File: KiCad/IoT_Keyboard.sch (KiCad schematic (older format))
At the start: 3 parts, among them SW1 SW_Push, U1 Elite-C

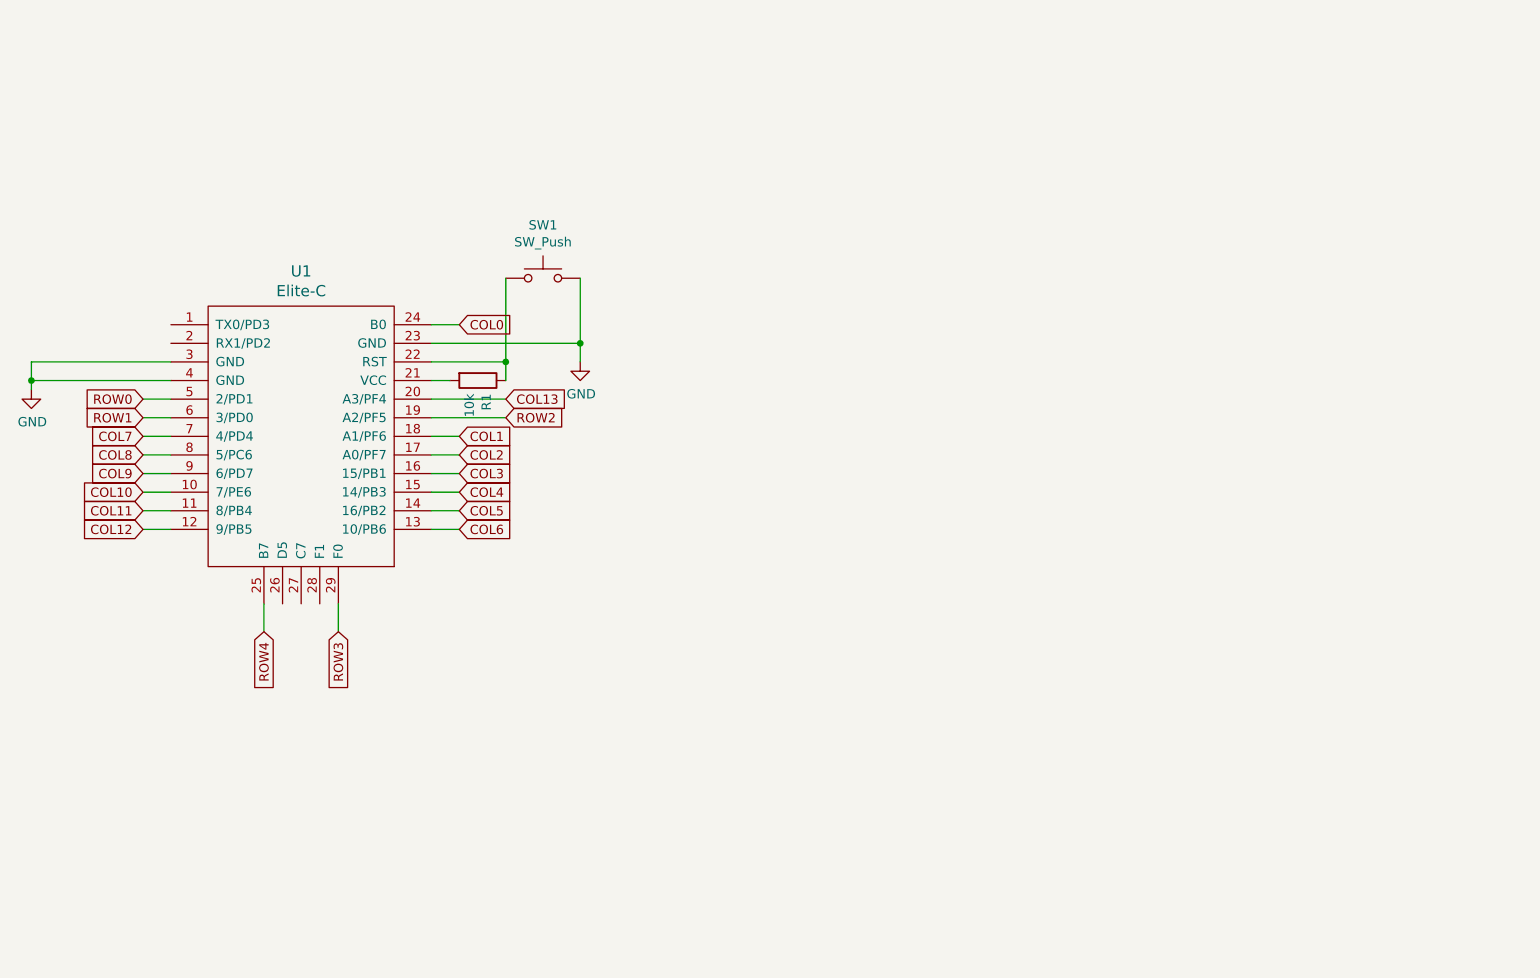
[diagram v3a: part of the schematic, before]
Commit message: Added HC-05 to PCB and routed. Added mounting holes. Generated gerbers
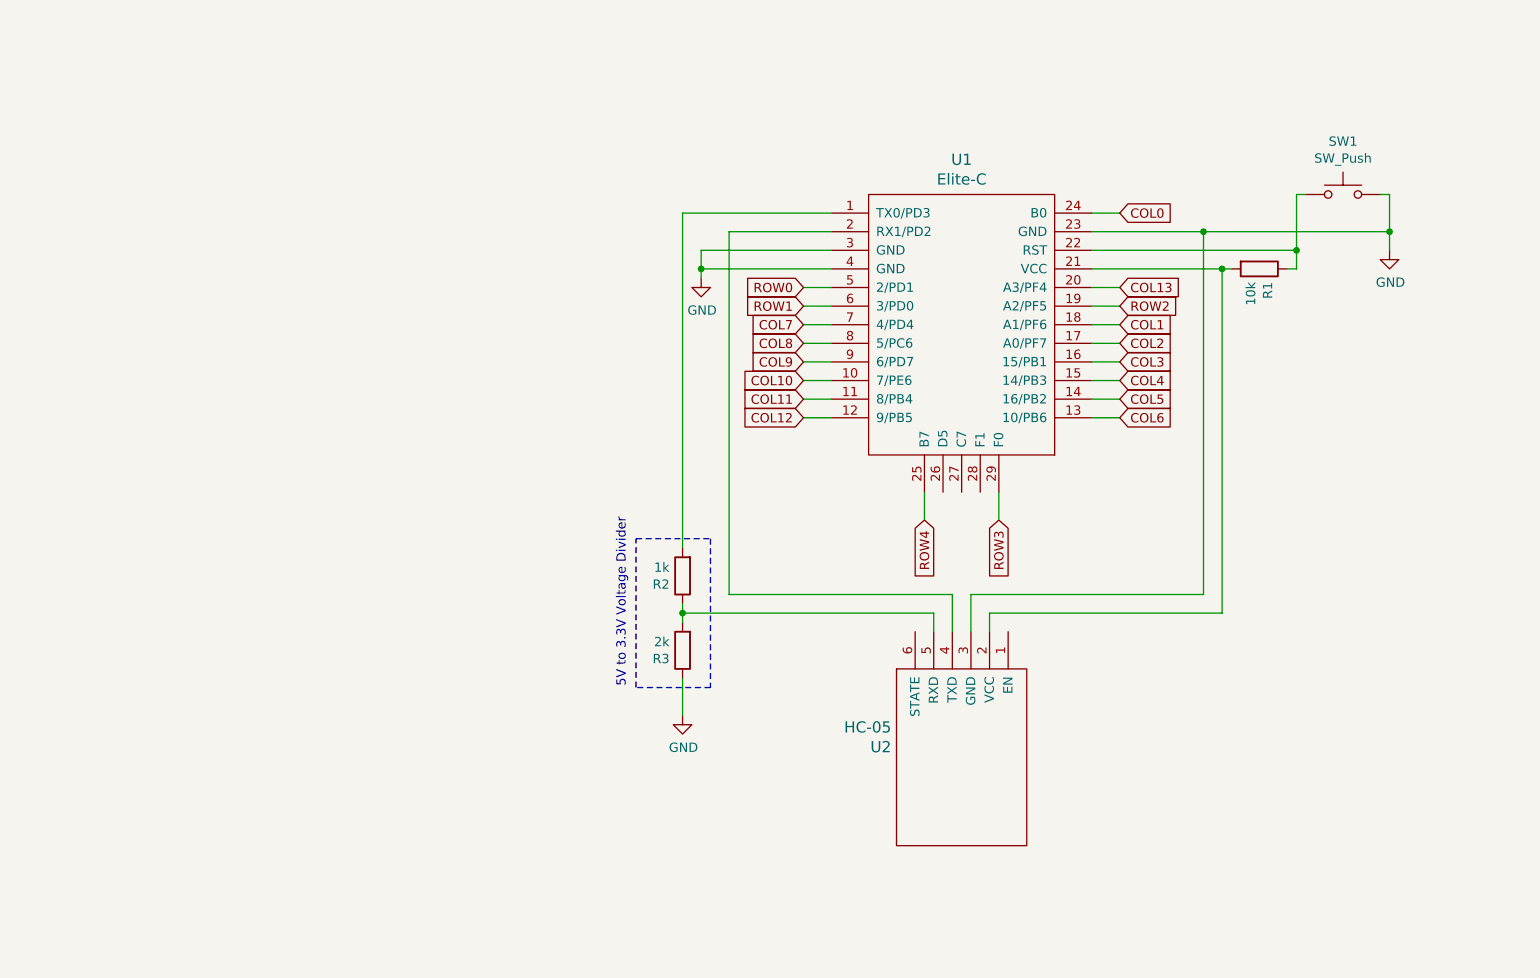
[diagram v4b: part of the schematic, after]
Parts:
- added R2: 1k, Resistor_SMD:R_0805_2012Metric, symbol Device:R
- added R3: 2k, Resistor_SMD:R_0805_2012Metric, symbol Device:R
- added U2: HC-05, Keebio:HC-05, symbol Keebio:HC-05
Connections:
- net GND: now also R3.1, U2.3 (GND)
- net at U1.1 (TX0/PD3): now also R2.2
- net at U1.2 (RX1/PD2): now also U2.4 (TXD)
- net at R1.2, U1.21 (VCC): now also U2.2 (VCC)
- new net: R2.1, R3.2, U2.5 (RXD)
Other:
- note added: "5V to 3.3V Voltage Divider"
- moved on the sheet: R1, SW1, U1
